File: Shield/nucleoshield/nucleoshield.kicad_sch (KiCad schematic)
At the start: 41 parts, among them IC1 L80-M39, J1 Conn_02x19_Odd_Even, J10 ENCODER_3, J11 MPU9250, J12 5V_DCDC, J13 3V3_DCDC, J2 Conn_02x19_Odd_Even, J3 Battery, J4 MOTOR_1, J5 ENCODER_1, J6 ENCODER_2, J7 MOTOR_2, J8 LCD_I2C, J9 MOTOR_3, Q1 BSS138, Q2 BSS138, Q3 AO3401A, Q4 AO3401A, Q5 AO3401A

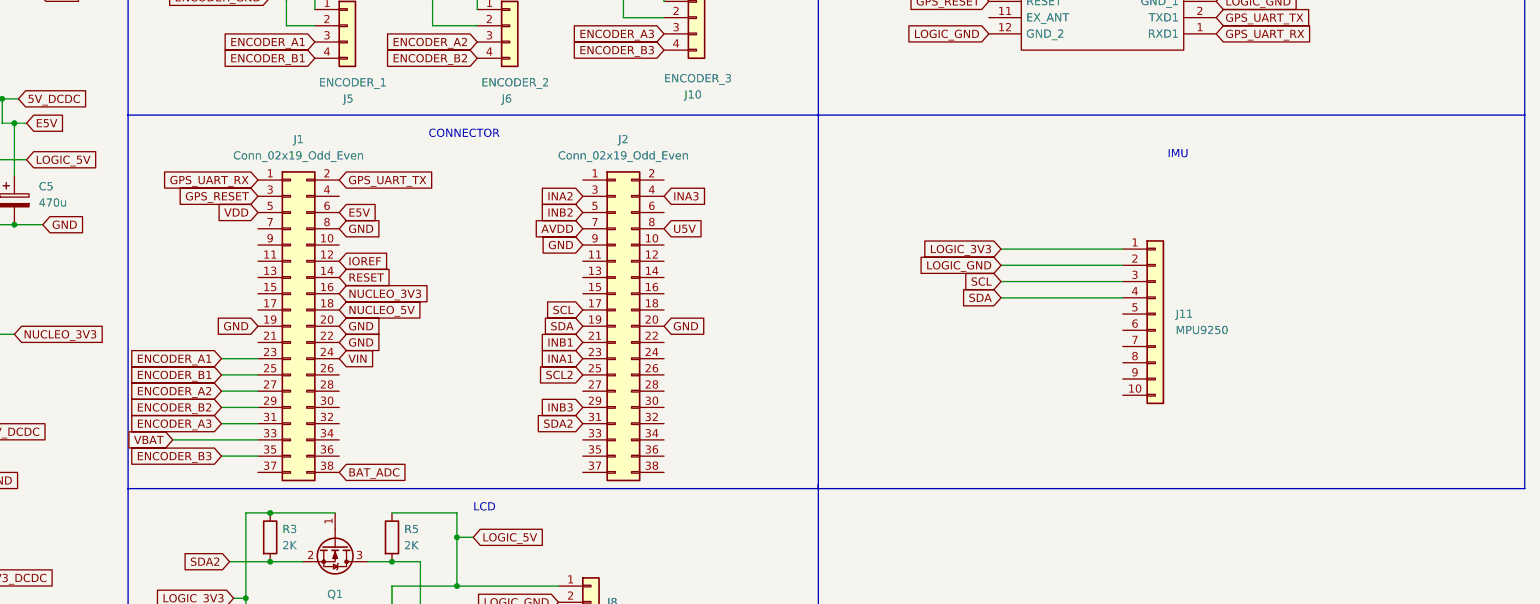
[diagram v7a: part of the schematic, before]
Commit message: Enkóderek timer bemenetekhez rendelve
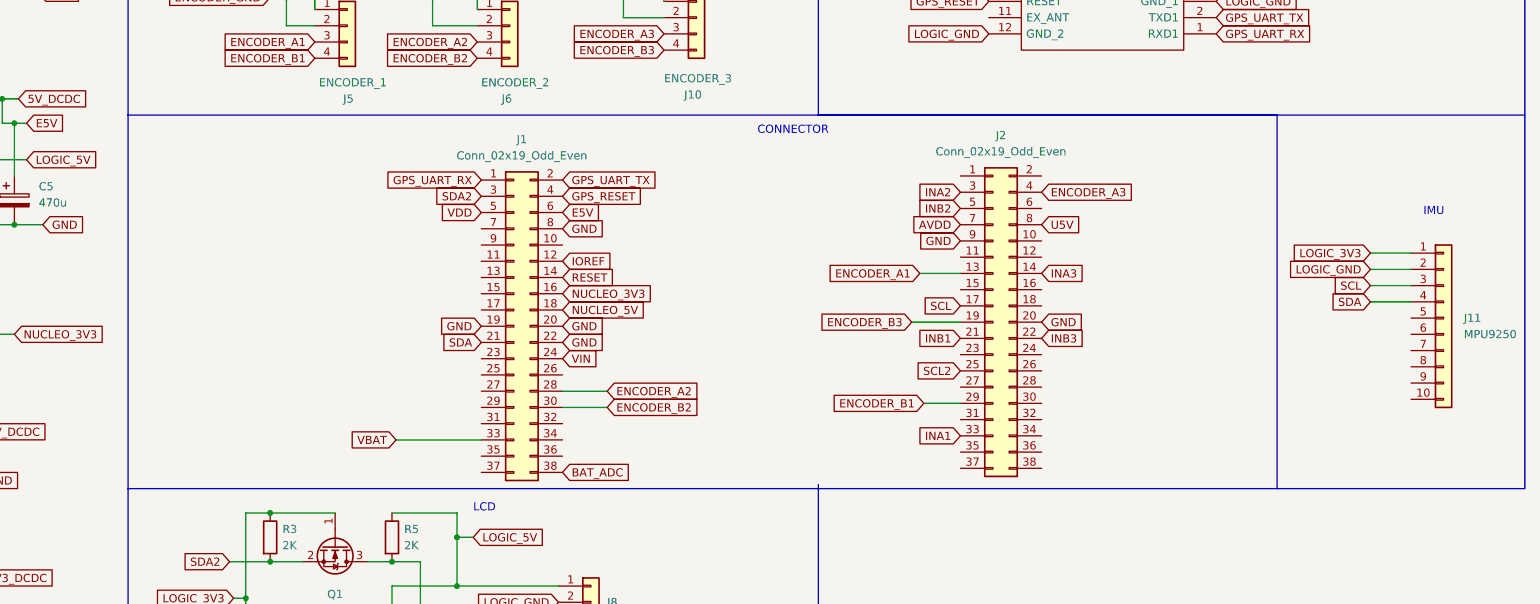
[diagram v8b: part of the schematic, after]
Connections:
- net ENCODER_A1: now also J2.13 (Pin_13); no longer J1.23 (Pin_23)
- net ENCODER_A2: now also J1.28 (Pin_28); no longer J1.27 (Pin_27)
- net ENCODER_A3: now also J2.4 (Pin_4); no longer J1.31 (Pin_31)
- net ENCODER_B1: now also J2.29 (Pin_29); no longer J1.25 (Pin_25)
- net ENCODER_B2: now also J1.30 (Pin_30); no longer J1.29 (Pin_29)
- net ENCODER_B3: now also J2.19 (Pin_19); no longer J1.35 (Pin_35)
- net GPS_RESET: now also J1.4 (Pin_4); no longer J1.3 (Pin_3)
- net INA1: now also J2.33 (Pin_33); no longer J2.23 (Pin_23)
- net INA3: now also J2.14 (Pin_14); no longer J2.4 (Pin_4)
- net INB3: now also J2.22 (Pin_22); no longer J2.29 (Pin_29)
- net SDA: now also J1.21 (Pin_21); no longer J2.19 (Pin_19)
- net SDA2: now also J1.3 (Pin_3); no longer J2.31 (Pin_31)
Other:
- moved on the sheet: J1, J11, J2
